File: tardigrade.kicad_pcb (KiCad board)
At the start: 4 copper layers, 77 x 56 mm, 147 parts, among them IC1 TPS63031, IC2 LPC55S16JBD64E, IC3 SX1262IMLTRT, IC4 PE4259-63, IC5 ATECC608A-TNGLORAU-B, J1 Conn_01x02, J2 Conn_01x02, J3 Conn_Coaxial, J4 Conn_Coaxial, J5 USB_C_Receptacle_USB2.0, J6 Conn_ARM_JTAG_SWD_10, J7 UART, J8 Conn_02x14_Top_Bottom, J9 RF Shield, SW1 KMR221NGLFS, SW2 KMR221NGLFS, U1 MCP73831T-2ACI/OT, U2 BQ25504, U3 MAX-8Q, U4 BAT-HLD-001, Y1 16 MHz, Y2 32.768 kHz, Y3 NT2016SA-32M-END4263A

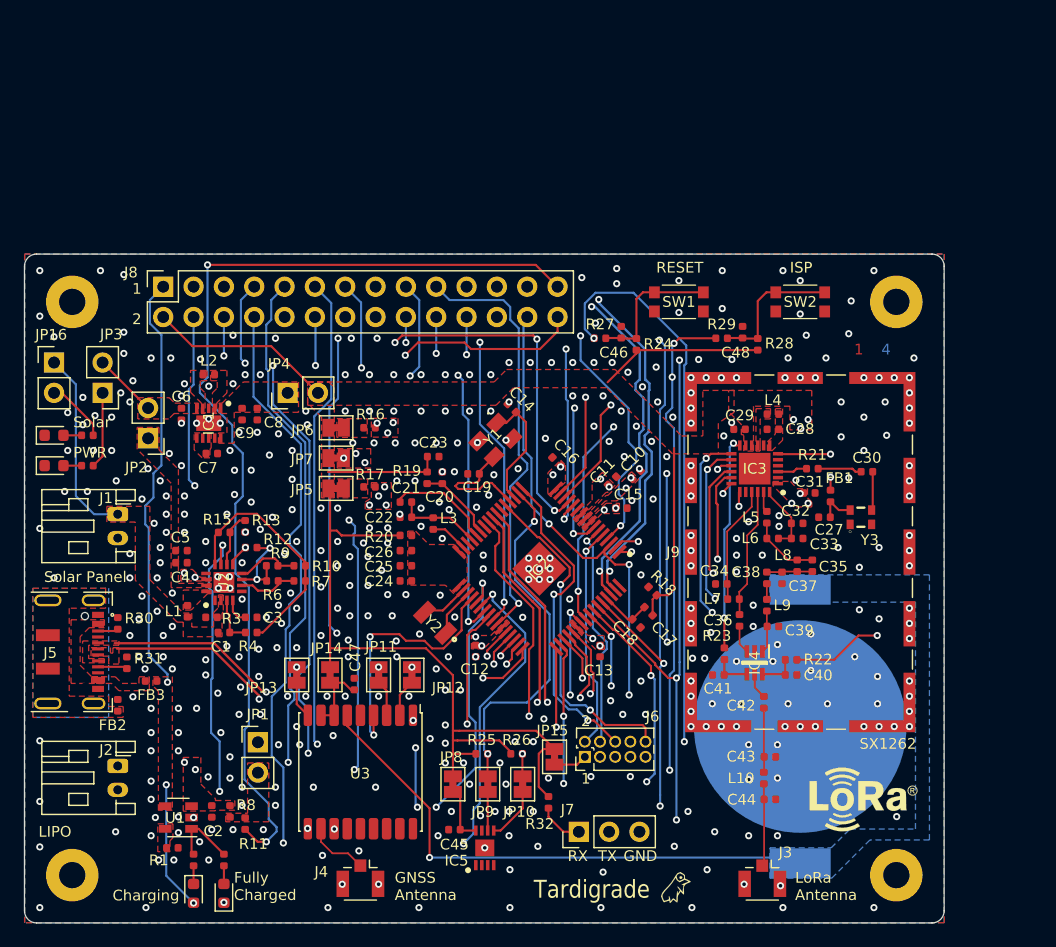
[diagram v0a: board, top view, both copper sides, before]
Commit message: Major change of the layout (reviewed) for V1.1
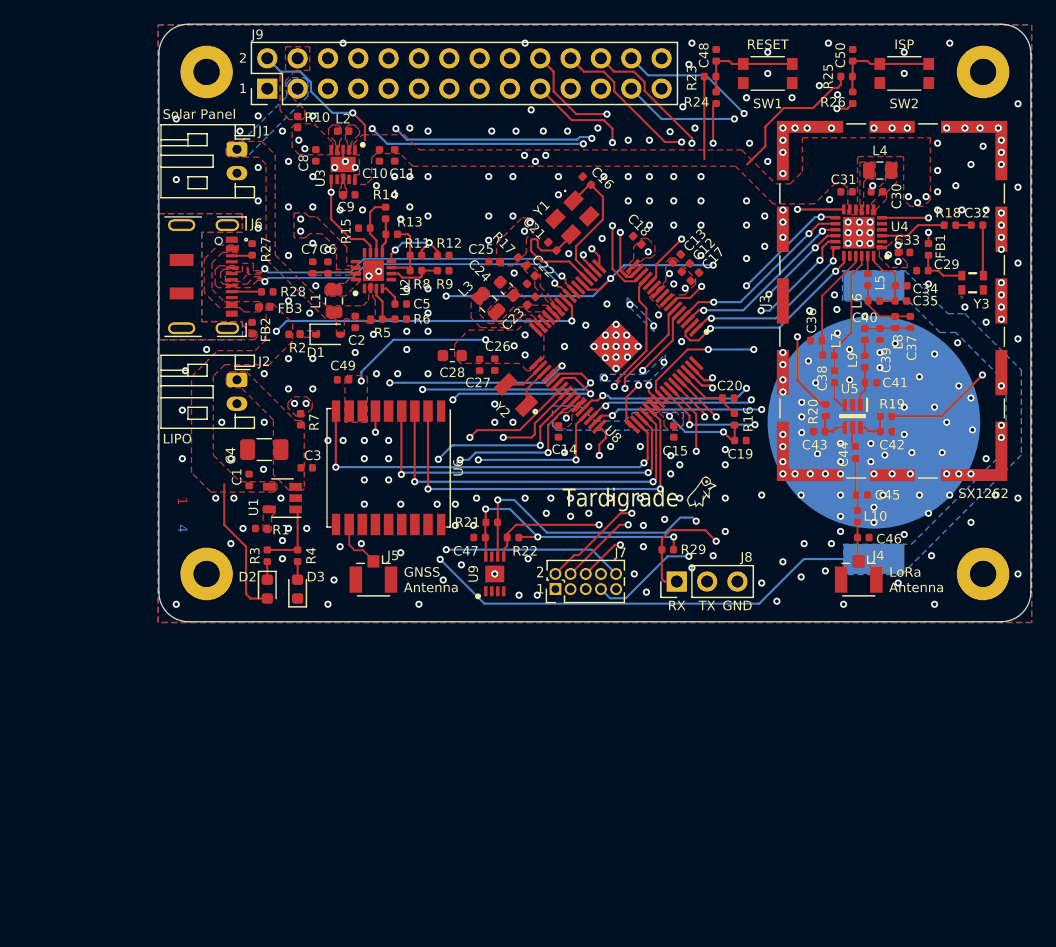
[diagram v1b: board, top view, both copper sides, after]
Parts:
- removed D4: LED, LED_SMD:LED_0603_1608Metric
- removed the G*** at (143.1, 59.1)
- removed the G*** at (166.4, 84.9)
- removed IC1: TPS63031, tardigrade-components:TPS63031DSKR
- removed IC2: LPC55S16JBD64E, tardigrade-components:QFP50P1200X1200X120-65N
- removed IC3: SX1262IMLTRT, tardigrade-components:QFN50P400X400X100-25N-D
- removed IC4: PE4259-63, tardigrade-components:SOT65P210X110-6N
- removed IC5: ATECC608A-TNGLORAU-B, tardigrade-components:SON50P300X200X60-9N
- removed JP1, JP16, JP2, JP3, JP4: Jumper_NC_Small, Connector_PinHeader_2.54mm:PinHeader_1x02_P2.54mm_Vertical
- removed JP10, JP11, JP12, JP13, JP14, JP15, JP5, JP6, JP7, JP8, JP9: Jumper_NC_Small, Jumper:SolderJumper-2_P1.3mm_Bridged_Pad1.0x1.5mm
- removed R30, R31: 5.1k, Resistor_SMD:R_0402_1005Metric
- removed R32: 10K, Resistor_SMD:R_0402_1005Metric
- removed R33: 100R, Resistor_SMD:R_0402_1005Metric
- removed the REF** at (142.1, 50.1)
- added C49: 0.1uF, Capacitor_SMD:C_0402_1005Metric, F.Cu at (123.0, 49.7)
- added C50: 0.01uF, Capacitor_SMD:C_0402_1005Metric, F.Cu at (165.7, 22.5)
- added G***: LOGO, tardigrade-components:public-repo-qr-code-big, B.Cu at (126.8, 36.8)
- added REF**: OSHW-Logo2_9.8x8mm_SilkScreen, Symbol:OSHW-Logo2_9.8x8mm_SilkScreen, B.Cu at (140.8, 32.9)
- added U5: PE4259-63, tardigrade-components:SOT65P210X110-6N, F.Cu at (165.7, 52.8)
- added U6: MAX-8Q, RF_GPS:ublox_MAX, F.Cu at (126.8, 57.1)
- added U7: BAT-HLD-001, tardigrade-components:BATHLD001, B.Cu at (167.5, 53.3)
- added U8: LPC55S16JBD64E, tardigrade-components:QFP50P1200X1200X120-65N, F.Cu at (145.9, 46.9)
- added U9: ATECC608A-TNGLORAU-B, tardigrade-components:SON50P300X200X60-9N, F.Cu at (135.7, 66.0)
- C1: value 4.7uH -> 10uF
- C10, C11: value 0.1uF -> 10uF
- C12, C17, C23: value 4.7uF -> 0.1uF
- C13: value 1.0uF -> 0.1uF
- C14, C19: value 12pF -> 4.7uF
- C15: value 0.1uF -> 1.0uF
- C16, C21: value 0.1uF -> 12pF
- C2: value 10uF -> 4.7uF
- C22: value 22uF -> 0.1uF
- C24: value 47pF -> 22uF; footprint Capacitor_SMD:C_0402_1005Metric -> Capacitor_SMD:C_0603_1608Metric
- C25, C7: value 0.1uF -> 4.7uF
- C26: value 22uF -> 47pF
- C28: value 470nF -> 22uF; footprint Capacitor_SMD:C_0402_1005Metric -> Capacitor_SMD:C_0603_1608Metric
- C3: value 0.01uF -> 10uF
- C30: value 10pF -> 470nF
- C31: value 1uF -> 0.1uF
- C32: value 47nF -> 10pF
- C33: value 47pF -> 1uF
- C34: value 1.8pF -> 47nF
- C35: value 3.3pF -> 47pF
- C36: value 2.4pF -> 1.8pF
- C37: value 5.6pF -> 3.3pF
- C38: value 39pF -> 2.4pF
- C39: value 2.2pF -> 5.6pF
- C4: value 0.1uF -> 150uF; footprint Capacitor_SMD:C_0402_1005Metric -> Capacitor_SMD:C_1206_3216Metric
- C40: value 1nF -> 39pF
- C41: value 1nF -> 2.2pF
- C42: value 39pF -> 1nF
- C43: value 3.3pF -> 1nF
- C44: value 3.3pF -> 39pF
- C45: value 0.1uF -> 3.3pF
- C46: value 0.01uF -> 3.3pF
- C5: value 4.7uF -> 0.01uF
- C6, C9: value 10uF -> 0.1uF
- D1: value LED -> ca. 2.2V; footprint LED_SMD:LED_0603_1608Metric -> Diode_SMD:D_SOD-323
- J3: value Conn_Coaxial -> RF Shield; footprint Connector_Coaxial:U.FL_Hirose_U.FL-R-SMT-1_Vertical -> RF_Shielding:Laird_Technologies_BMI-S-209-F_29.36x18.50mm
- J5: value USB_C_Receptacle_USB2.0 -> Conn_Coaxial; footprint tardigrade-components:USB_C_Receptacle_JAE_DX07S016JA1 -> Connector_Coaxial:U.FL_Hirose_U.FL-R-SMT-1_Vertical
- J6: value Conn_ARM_JTAG_SWD_10 -> USB_C_Receptacle_USB2.0; footprint Connector_PinHeader_1.27mm:PinHeader_2x05_P1.27mm_Vertical -> tardigrade-components:USB_C_Receptacle_JAE_DX07S016JA1
- J7: value UART -> Conn_ARM_JTAG_SWD_10; footprint Connector_PinHeader_2.54mm:PinHeader_1x03_P2.54mm_Vertical -> Connector_PinHeader_1.27mm:PinHeader_2x05_P1.27mm_Vertical
- J8: value Conn_02x14_Top_Bottom -> UART; footprint Connector_PinSocket_2.54mm:PinSocket_2x14_P2.54mm_Vertical -> Connector_PinHeader_2.54mm:PinHeader_1x03_P2.54mm_Vertical
- J9: value RF Shield -> Conn_02x14_Odd_Even; footprint RF_Shielding:Laird_Technologies_BMI-S-209-F_29.36x18.50mm -> Connector_PinHeader_2.54mm:PinHeader_2x14_P2.54mm_Vertical
- L1: value 22uH1 -> 22uH; footprint Inductor_SMD:L_0402_1005Metric -> Inductor_SMD:L_0805_2012Metric
- L3, L4: footprint Inductor_SMD:L_0402_1005Metric -> Inductor_SMD:L_0805_2012Metric
- R1: value 10K -> 5.1k
- R10: value 4.12M -> 0R
- R11, R8: value 0R -> 5.49M
- R12: value 2.43M -> 4.42M
- R13: value 4.42M -> 0.316M
- R14: value 100R -> 5.62M
- R15: value 3.01M -> 4.02M
- R18: value 0R -> 220R
- R19, R20: value 0R -> 100R
- R2: value 1K -> 150R
- R21: value 220R -> 10K
- R22: value 100R -> 10K
- R23: value 100R -> 100K
- R24: value 100K -> 1K
- R25: value 10K -> 100K
- R26: value 10K -> 1K
- R27: value 1K -> 5.1k
- R28: value 100K -> 5.1k
- R29: value 1K -> 10K
- R3: value 4.02M -> 1K
- R4: value 6.04M -> 1K
- R5: value 1K -> 4.02M
- R6: value 5.49M -> 6.04M
- R7: value 4.53M -> 0R
- R9: value 5.76M -> 4.53M
- U3: value MAX-8Q -> TPS63031; footprint RF_GPS:ublox_MAX -> tardigrade-components:TPS63031DSKR
- U4: value BAT-HLD-001 -> SX1262IMLTRT; footprint tardigrade-components:BATHLD001 -> tardigrade-components:QFN50P400X400X100-25N-D; moved to F.Cu
- moved H3 101.7 mm to (176.6, 23.9)
- moved H4 88.7 mm to (111.6, 23.9)
- moved H1 79.6 mm to (176.6, 66.0)
- moved R25 64.4 mm to (165.2, 24.3), turned to 180 degrees
- moved H2 62.1 mm to (111.6, 66.0)
- moved R26 61.7 mm to (165.7, 26.1), turned to 90 degrees
- moved J9 59.1 mm to (116.7, 25.3)
- moved J6 51.3 mm to (111.3, 41.1), turned to 270 degrees
- moved U3 50.9 mm to (123.0, 31.7)
- moved R11 49.7 mm to (129.1, 39.3), turned to 180 degrees
- moved J8 49.6 mm to (151.0, 66.6)
- moved J3 49.5 mm to (169.0, 43.1), turned to 90 degrees
- moved J4 48.9 mm to (166.2, 66.0)
- moved R23 48.4 mm to (153.7, 24.3), turned to 180 degrees
- moved D1 48.1 mm to (121.7, 45.9), turned to 0 degrees
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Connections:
- C1 pad 1: EXT_VIN -> VBUS
- C1 pad 2: GND -> BQ_AVSS
- C10 pad 1: Net-(C10-Pad1) -> MCU_VBAT_PMU
- C10 pad 2: GND -> BQ_AVSS
- C11 pad 1: MCU_VREF -> MCU_VBAT_PMU
- C11 pad 2: GND -> BQ_AVSS
- C12 pad 1: Net-(C12-Pad1) -> MCU_VBAT_PMU
- C12 pad 2: GND -> BQ_AVSS
- C13 pad 1: Net-(C12-Pad1) -> MCU_VBAT_PMU
- C13 pad 2: GND -> BQ_AVSS
- C14 pad 1: Net-(C14-Pad1) -> MCU_VBAT_PMU
- C14 pad 2: GND -> BQ_AVSS
- C15 pad 1: Net-(C12-Pad1) -> MCU_VBAT_PMU
- C15 pad 2: GND -> BQ_AVSS
- C16 pad 1: Net-(C12-Pad1) -> Net-(C16-Pad1)
- C16 pad 2: GND -> BQ_AVSS
- C17 pad 1: SX_VDD -> MCU_VBAT_PMU
- C17 pad 2: GND -> BQ_AVSS
- C18 pad 1: Net-(C18-Pad1) -> MCU_VBAT_PMU
- C18 pad 2: GND -> BQ_AVSS
- C19 pad 1: Net-(C19-Pad1) -> MCU_VBAT_PMU
- C19 pad 2: GND -> BQ_AVSS
- C2 pad 1: Net-(C2-Pad1) -> EXT_VIN
- C2 pad 2: GND -> BQ_AVSS
- C20 pad 2: GND -> BQ_AVSS
- C21 pad 2: Net-(C21-Pad2) -> BQ_AVSS
- C22 pad 1: Net-(C21-Pad2) -> Net-(C22-Pad1)
- C22 pad 2: GND -> BQ_AVSS
- C23 pad 1: SX_VDD -> Net-(C23-Pad1)
- C23 pad 2: GND -> BQ_AVSS
- C24 pad 1: Net-(C24-Pad1) -> Net-(C23-Pad1)
- C24 pad 2: GND -> BQ_AVSS
- C25 pad 1: Net-(C24-Pad1) -> MCU_VBAT_PMU
- C25 pad 2: GND -> BQ_AVSS
- C26 pad 1: Net-(C24-Pad1) -> MCU_VBAT_PMU
- C26 pad 2: GND -> BQ_AVSS
- C27 pad 1: GND -> MCU_VBAT_PMU
- C27 pad 2: Net-(C27-Pad2) -> BQ_AVSS
- C28 pad 1: GND -> MCU_VBAT_PMU
- C28 pad 2: Net-(C28-Pad2) -> BQ_AVSS
- C29 pad 1: GND -> BQ_AVSS
- C29 pad 2: SX_VDD -> Net-(C29-Pad2)
- C3 pad 2: GND -> BQ_AVSS
- C30 pad 1: Net-(C30-Pad1) -> BQ_AVSS
- C31 pad 1: GND -> BQ_AVSS
- C31 pad 2: SX_VDD -> MCU_VBAT_PMU
- C32 pad 1: GND -> Net-(C32-Pad1)
- C33 pad 1: GND -> BQ_AVSS
- C33 pad 2: Net-(C32-Pad2) -> MCU_VBAT_PMU
- C34 pad 1: GND -> BQ_AVSS
- C35 pad 1: Net-(C35-Pad1) -> BQ_AVSS
- C35 pad 2: Net-(C35-Pad2) -> Net-(C34-Pad2)
- C36 pad 1: Net-(C36-Pad1) -> BQ_AVSS
- C37 pad 1: GND -> Net-(C37-Pad1)
- C37 pad 2: Net-(C35-Pad1) -> Net-(C37-Pad2)
- C38 pad 2: Net-(C35-Pad1) -> Net-(C38-Pad2)
- C39 pad 1: GND -> BQ_AVSS
- C39 pad 2: Net-(C39-Pad2) -> Net-(C37-Pad1)
- C4 pad 1: Net-(C4-Pad1) -> BQ_AVSS
- C4 pad 2: GND -> Net-(C3-Pad1)
- C40 pad 1: GND -> Net-(C40-Pad1)
- C40 pad 2: Net-(C40-Pad2) -> Net-(C37-Pad1)
- C41 pad 1: GND -> BQ_AVSS
- C42 pad 1: Net-(C42-Pad1) -> BQ_AVSS
- C43 pad 1: GND -> BQ_AVSS
- C43 pad 2: Net-(C42-Pad1) -> Net-(C43-Pad2)
- C44 pad 1: GND -> Net-(C44-Pad1)
- C45 pad 1: Net-(C45-Pad1) -> BQ_AVSS
- C45 pad 2: GND -> Net-(C44-Pad1)
- C46 pad 1: Net-(C46-Pad1) -> BQ_AVSS
- C46 pad 2: GND -> Net-(C46-Pad2)
- C47 pad 1: Net-(C47-Pad1) -> MCU_VBAT_PMU
- C47 pad 2: GND -> BQ_AVSS
- C48 pad 2: GND -> BQ_AVSS
- C5 pad 1: Net-(C4-Pad1) -> Net-(C5-Pad1)
- C5 pad 2: GND -> BQ_AVSS
- C6 pad 2: GND -> BQ_AVSS
- C7 pad 1: Net-(C7-Pad1) -> Net-(C6-Pad1)
- C7 pad 2: GND -> BQ_AVSS
- C8 pad 2: GND -> BQ_AVSS
- C9 pad 1: Net-(C8-Pad1) -> Net-(C9-Pad1)
- C9 pad 2: GND -> BQ_AVSS
- D1 pad 2: VBUS -> EXT_VIN
- D2 pad 1: GND -> Net-(D2-Pad1)
- D2 pad 2: Net-(D2-Pad2) -> VBUS
- D3 pad 1: GND -> BQ_AVSS
- FB1 pad 1: Net-(C27-Pad2) -> Net-(C29-Pad2)
- FB2 pad 2: GND -> BQ_AVSS
- J1 pad 2: GND -> BQ_AVSS
- J2 pad 1: Net-(C2-Pad1) -> Net-(C3-Pad1)
- J2 pad 2: GND -> BQ_AVSS
- J3 pad 1: Net-(C44-Pad2) -> BQ_AVSS
- J4 pad 1: Net-(J4-Pad1) -> Net-(C46-Pad2)
- J4 pad 2: GND -> BQ_AVSS
- J7 pad 1: MCU_UART_TX -> MCU_VBAT_PMU
- J7 pad 2: MCU_UART_RX -> MCU_SWDIO
- J7 pad 3: GND -> BQ_AVSS
- J8 pad 1: VBUS -> MCU_UART_TX
- J8 pad 2: SX_VDD -> MCU_UART_RX
- J8 pad 3: GND -> BQ_AVSS
- J9 pad 1: GND -> VBUS
- L10 pad 1: Net-(C42-Pad1) -> Net-(C44-Pad1)
- L10 pad 2: Net-(C44-Pad2) -> Net-(C46-Pad2)
- L2 pad 1: Net-(IC1-Pad4) -> Net-(L2-Pad1)
- L2 pad 2: Net-(IC1-Pad2) -> Net-(L2-Pad2)
- L3 pad 1: Net-(C21-Pad2) -> Net-(C23-Pad1)
- L4 pad 1: Net-(IC3-Pad9) -> Net-(L4-Pad1)
- L4 pad 2: Net-(C28-Pad2) -> Net-(C30-Pad2)
- L5 pad 1: Net-(IC3-Pad23) -> Net-(L5-Pad1)
- L5 pad 2: Net-(C35-Pad2) -> Net-(C37-Pad2)
- L6 pad 1: Net-(C35-Pad2) -> Net-(C37-Pad2)
- L6 pad 2: Net-(C32-Pad2) -> Net-(C34-Pad2)
- L7 pad 1: Net-(C34-Pad2) -> Net-(C36-Pad2)
- L7 pad 2: Net-(C36-Pad2) -> Net-(C38-Pad2)
- L8 pad 1: Net-(C35-Pad2) -> Net-(C37-Pad2)
- L8 pad 2: Net-(C35-Pad1) -> Net-(C37-Pad1)
- L9 pad 1: Net-(C38-Pad1) -> Net-(C40-Pad1)
- L9 pad 2: Net-(C39-Pad2) -> Net-(C41-Pad2)
- R1 pad 1: GND -> BQ_AVSS
- R10 pad 1: BQ_AVSS -> EXT_VBAT
- R10 pad 2: Net-(R10-Pad2) -> Net-(C8-Pad1)
- R11 pad 1: EXT_VBAT -> Net-(R11-Pad1)
- R11 pad 2: Net-(JP1-Pad2) -> Net-(R11-Pad2)
- R12 pad 1: Net-(R12-Pad1) -> BQ_AVSS
- R12 pad 2: Net-(R12-Pad2) -> Net-(R11-Pad1)
- R13 pad 1: Net-(R12-Pad1) -> Net-(R13-Pad1)
- R13 pad 2: Net-(R13-Pad2) -> Net-(R11-Pad2)
- R14 pad 1: Net-(D3-Pad2) -> Net-(R13-Pad1)
- R14 pad 2: Net-(JP3-Pad1) -> Net-(R14-Pad2)
- R15 pad 1: Net-(R13-Pad2) -> Net-(R14-Pad2)
- R16 pad 1: Net-(C10-Pad1) -> Net-(C20-Pad1)
- R16 pad 2: MCU_VDDA -> MCU_VBAT_PMU
- R17 pad 1: Net-(C12-Pad1) -> MCU_VBAT_PMU
- R17 pad 2: MCU_VDD -> Net-(C22-Pad1)
- R18 pad 1: Net-(C18-Pad1) -> Net-(R18-Pad1)
- R18 pad 2: SX_VDD -> Net-(C32-Pad1)
- R19 pad 1: SX_VDD -> Net-(C42-Pad2)
- R19 pad 2: Net-(C20-Pad1) -> LORA_ANT_SW
- R2 pad 1: Net-(D1-Pad1) -> VBUS
- R2 pad 2: Net-(R2-Pad2) -> Net-(D1-Pad1)
- R20 pad 1: SX_VDD -> Net-(C43-Pad2)
- R20 pad 2: Net-(C24-Pad1) -> SX1262_DIO2
- R21 pad 1: Net-(IC3-Pad3) -> MCU_VBAT_PMU
- R21 pad 2: Net-(C30-Pad1) -> SE_SCL
- R22 pad 1: Net-(C40-Pad2) -> MCU_VBAT_PMU
- R22 pad 2: LORA_ANT_SW -> SE_SDA
- R23 pad 1: Net-(C41-Pad2) -> Net-(C48-Pad1)
- R23 pad 2: SX1262_DIO2 -> MCU_VBAT_PMU
- R24 pad 1: Net-(C46-Pad1) -> MCU_RESET
- R24 pad 2: SX_VDD -> Net-(C48-Pad1)
- R25 pad 1: SX_VDD -> Net-(C50-Pad1)
- R25 pad 2: SE_I2C_SCL -> MCU_VBAT_PMU
- R26 pad 1: SX_VDD -> MCU_ISP_MODE
- R26 pad 2: SE_I2C_SDA -> Net-(C50-Pad1)
- R27 pad 1: MCU_RESET -> BQ_AVSS
- R27 pad 2: Net-(C46-Pad1) -> Net-(J6-PadA5)
- R28 pad 1: Net-(C48-Pad1) -> BQ_AVSS
- R28 pad 2: SX_VDD -> Net-(J6-PadB5)
- R29 pad 1: MCU_ISP_MODE -> MCU_UART_TX
- R29 pad 2: Net-(C48-Pad1) -> MCU_VBAT_PMU
- R3 pad 1: EXT_VIN -> Net-(D2-Pad1)
- R4 pad 1: Net-(R3-Pad2) -> Net-(D3-Pad2)
- R4 pad 2: BQ_AVSS -> Net-(R3-Pad2)
- R5 pad 1: Net-(D2-Pad2) -> EXT_VIN
- R5 pad 2: Net-(R2-Pad2) -> Net-(R5-Pad2)
- R6 pad 1: Net-(R6-Pad1) -> Net-(R5-Pad2)
- R6 pad 2: Net-(R12-Pad2) -> BQ_AVSS
- R7 pad 1: BQ_AVSS -> Net-(C3-Pad1)
- R7 pad 2: Net-(R6-Pad1) -> Net-(C8-Pad1)
- R8 pad 1: Net-(C2-Pad1) -> Net-(R8-Pad1)
- R8 pad 2: Net-(JP1-Pad2) -> Net-(R11-Pad2)
- R9 pad 1: Net-(R10-Pad2) -> BQ_AVSS
- R9 pad 2: Net-(R12-Pad2) -> Net-(R8-Pad1)
- SW1 pad 1: Net-(C46-Pad1) -> Net-(C48-Pad1)
- SW1 pad 2: Net-(C46-Pad1) -> Net-(C48-Pad1)
- SW1 pad 3: GND -> BQ_AVSS
- SW1 pad 4: GND -> BQ_AVSS
- SW2 pad 1: Net-(C48-Pad1) -> Net-(C50-Pad1)
- SW2 pad 2: Net-(C48-Pad1) -> Net-(C50-Pad1)
- SW2 pad 3: GND -> BQ_AVSS
- SW2 pad 4: GND -> BQ_AVSS
- U1 pad 1: Net-(R2-Pad2) -> Net-(R3-Pad2)
- U1 pad 2: GND -> BQ_AVSS
- U1 pad 3: Net-(C2-Pad1) -> Net-(C3-Pad1)
- U2 pad 1: GND -> BQ_AVSS
- U2 pad 10: Net-(R13-Pad2) -> Net-(R14-Pad2)
- U2 pad 13: GND -> BQ_AVSS
- U2 pad 14: Net-(JP1-Pad1) -> Net-(C8-Pad1)
- U2 pad 15: Net-(C4-Pad1) -> Net-(C6-Pad1)
- U2 pad 17: GND -> BQ_AVSS
- U2 pad 3: Net-(R3-Pad2) -> Net-(R5-Pad2)
- U2 pad 4: Net-(C3-Pad1) -> Net-(C5-Pad1)
- U2 pad 5: GND -> BQ_AVSS
- U2 pad 6: Net-(R6-Pad1) -> Net-(R8-Pad1)
- U2 pad 7: Net-(R12-Pad2) -> Net-(R11-Pad2)
- U2 pad 8: Net-(R10-Pad2) -> Net-(R11-Pad1)
- U2 pad 9: Net-(R12-Pad1) -> Net-(R13-Pad1)
- U3 pad 1: GND -> MCU_VBAT_PMU
- U3 pad 10: GND -> MCU_VBAT_PMU
- U3 pad 11: Net-(J4-Pad1) -> BQ_AVSS
- U3 pad 2: Net-(JP12-Pad2) -> Net-(L2-Pad2)
- U3 pad 3: Net-(JP11-Pad2) -> BQ_AVSS
- U3 pad 4: GNSS_PPS -> Net-(L2-Pad1)
- U3 pad 5: Net-(U3-Pad5) -> Net-(C8-Pad1)
- U3 pad 6: Net-(U3-Pad6) -> VBAT_OK
- U3 pad 7: Net-(C47-Pad1) -> BQ_AVSS
- U3 pad 8: Net-(C47-Pad1) -> Net-(C9-Pad1)
- U3 pad 9: Net-(JP13-Pad2) -> BQ_AVSS
- U4 pad 1: Net-(U3-Pad6) -> MCU_VBAT_PMU
- U4 pad 2: Net-(U3-Pad6) -> BQ_AVSS
- U4 pad 3: GND -> Net-(R18-Pad1)
- Y1 pad 1: Net-(C14-Pad1) -> Net-(C16-Pad1)
- Y1 pad 2: GND -> BQ_AVSS
- Y1 pad 3: Net-(C19-Pad1) -> Net-(C21-Pad1)
- Y1 pad 4: GND -> BQ_AVSS
- Y3 pad 1: GND -> BQ_AVSS
- Y3 pad 2: GND -> BQ_AVSS
- Y3 pad 3: Net-(C30-Pad2) -> Net-(C32-Pad2)
- Y3 pad 4: Net-(C27-Pad2) -> Net-(C29-Pad2)
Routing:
- net SX_VDD: track 116.9 -> 0.00 mm, vias 6 -> 0
- net MCU_VBAT_PMU: track 0.00 -> 94.1 mm, vias 0 -> 31
- net MCU_PIO0_19: track 91.4 -> 0.00 mm, vias 3 -> 0
- net VBAT_OK: track 106.7 -> 16.9 mm, vias 7 -> 1
- net EXT_VBAT: track 84.7 -> 0.00 mm, vias 2 -> 0
- net MCU_PIO0_22: track 77.2 -> 0.00 mm, vias 5 -> 0
- net EXT_VIN: track 61.9 -> 0.00 mm, vias 1 -> 0
- net Net-(U6-Pad6): track 0.00 -> 54.1 mm, vias 0 -> 2
- net MCU_PIO0_20: track 50.6 -> 0.00 mm, vias 3 -> 0
- net MCU_PIO0_24: track 0.00 -> 47.8 mm, vias 0 -> 2
- net MCU_PIO0_18: track 88.5 -> 41.5 mm, vias 3 -> 2
- net Net-(U3-Pad6): track 46.0 -> 0.00 mm, vias 1 -> 0
- net MCU_PIO0_10: track 45.7 -> 0.00 mm, vias 3 -> 0
- net MCU_PIO0_0: track 0.00 -> 41.2 mm, vias 0 -> 2
- net MCU_PIO1_0: track 38.2 -> 0.00 mm, vias 2 -> 0
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- added copper zone on B.Cu, net BQ_AVSS
- added copper zone on F.Cu, net BQ_AVSS
- added copper zone on In1.Cu, net BQ_AVSS
- added copper zone on In2.Cu, net BQ_AVSS
- added copper zone on F.Cu, net EXT_VBAT
- added copper zone on B.Cu, net EXT_VIN
- added copper zone on B.Cu, net MCU_VBAT_PMU
- added copper zone on F.Cu, net MCU_VBAT_PMU
- added copper zone on In1.Cu, net MCU_VBAT_PMU
- added copper zone on In2.Cu, net MCU_VBAT_PMU
- added copper zone on F.Cu, net Net-(C22-Pad1)
- added copper zone on F.Cu, net Net-(C23-Pad1)
- added copper zone on F.Cu, net Net-(C3-Pad1)
- added copper zone on F.Cu, net Net-(C30-Pad2)
- added copper zone on In2.Cu, net Net-(C8-Pad1)
- added copper zone on F.Cu, net Net-(C9-Pad1)
- added copper zone on F.Cu, net Net-(D1-Pad1)
- added copper zone on F.Cu, net Net-(L2-Pad1)
- added copper zone on F.Cu, net Net-(L2-Pad2)
- added copper zone on F.Cu, net Net-(L3-Pad2)
- added copper zone on F.Cu, net Net-(L4-Pad1)
- added copper zone on B.Cu, net Net-(U6-Pad6)
- removed copper zone on B.Cu, net GND
- removed copper zone on F.Cu, net GND
- removed copper zone on In1.Cu, net GND
- removed copper zone on In2.Cu, net GND
- removed copper zone on F.Cu, net MCU_VDD
- removed copper zone on F.Cu, net MCU_VDDA
- removed copper zone on F.Cu, net MCU_VREF
- removed copper zone on In2.Cu, net MCU_VREF
- removed copper zone on F.Cu, net Net-(C10-Pad1)
- removed copper zone on In2.Cu, net Net-(C10-Pad1)
- removed copper zone on F.Cu, net Net-(C12-Pad1)
- removed copper zone on In2.Cu, net Net-(C12-Pad1)
- removed copper zone on F.Cu, net Net-(C2-Pad1)
- removed copper zone on In2.Cu, net Net-(C2-Pad1)
- removed copper zone on F.Cu, net Net-(C24-Pad1)
- removed copper zone on F.Cu, net Net-(C28-Pad2)
- removed copper zone on F.Cu, net Net-(C4-Pad1)
- removed copper zone on F.Cu, net Net-(C7-Pad1)
- removed copper zone on F.Cu, net Net-(IC1-Pad2)
- removed copper zone on F.Cu, net Net-(IC1-Pad4)
- removed copper zone on F.Cu, net Net-(IC3-Pad9)
- removed copper zone on F.Cu, net Net-(JP1-Pad1)
- removed copper zone on In2.Cu, net Net-(JP1-Pad1)
- removed copper zone on F.Cu, net Net-(JP1-Pad2)
- removed copper zone on B.Cu, net Net-(U3-Pad6)
- removed copper zone on F.Cu, net SX_VDD
- removed copper zone on In1.Cu, net SX_VDD
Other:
- board size 77 x 56 mm -> 73 x 50 mm
- board text added: "V 1.1, November 2020 Diego Bienz"
- board text removed: "Charging"
- board text removed: "Fully Charged"
- board text removed: "PWR"
- board text removed: "Solar"
- board text removed: "V 1.0, October 2020 Diego Bienz"
